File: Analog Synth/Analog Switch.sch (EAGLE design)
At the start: 15 parts, among them IC1 TL082P, Q1 J310, T3 2N3904

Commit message: working on senior design and analog switch
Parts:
- added R4: 100k, resistor:R-US_0204/2V
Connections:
- new net N$7: D3.A, IC1B.+IN, R4.1
- net +12V: now also R4.2; no longer D3.A, IC1B.-IN
- net N$4: now also IC1B.-IN; no longer IC1B.+IN
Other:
- moved on the sheet: IC1B
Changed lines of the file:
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@@
 <part name="P-1" library="supply1" deviceset="-12V" device=""/>
 <part name="SUPPLY5" library="supply2" deviceset="GND" device=""/>
+<part name="R4" library="resistor" deviceset="R-US_" device="0204/2V" value="100k"/>
 </parts>
 <sheets>
@@
 </instance>
 <instance part="SUPPLY3" gate="GND" x="10.16" y="40.64"/>
-<instance part="P+1" gate="1" x="17.78" y="66.04"/>
+<instance part="P+1" gate="1" x="17.78" y="73.66"/>
 <instance part="R6" gate="G$1" x="71.12" y="76.2" smashed="yes" rot="R270">
 <attribute name="NAME" x="67.5894" y="74.422" size="1.778" layer="95" rot="R90"/>
@@
 <instance part="SUPPLY7" gate="GND" x="111.76" y="35.56"/>
 <instance part="SUPPLY8" gate="GND" x="88.9" y="35.56"/>
-<instance part="IC1" gate="B" x="27.94" y="53.34"/>
+<instance part="IC1" gate="B" x="27.94" y="53.34" rot="MR180"/>
 <instance part="D3" gate="1" x="17.78" y="45.72" smashed="yes" rot="R270">
 <attribute name="NAME" x="19.5326" y="47.244" size="1.778" layer="95" rot="R270"/>
@@
 <instance part="P-1" gate="1" x="55.88" y="25.4"/>
 <instance part="SUPPLY5" gate="GND" x="40.64" y="25.4"/>
+<instance part="R4" gate="G$1" x="17.78" y="63.5" smashed="yes" rot="R90">
+<attribute name="NAME" x="13.7414" y="61.976" size="1.778" layer="95" rot="R90"/>
+<attribute name="VALUE" x="16.002" y="60.706" size="1.778" layer="96" rot="R90"/>
+</instance>
 </instances>
 <busses>
@@
 <net name="+12V" class="0">
 <segment>
-<pinref part="P+1" gate="1" pin="+12V"/>
-<wire x1="17.78" y1="50.8" x2="17.78" y2="63.5" width="0.1524" layer="91"/>
-<pinref part="IC1" gate="B" pin="-IN"/>
-<wire x1="20.32" y1="50.8" x2="17.78" y2="50.8" width="0.1524" layer="91"/>
-<pinref part="D3" gate="1" pin="A"/>
-<wire x1="17.78" y1="50.8" x2="17.78" y2="48.26" width="0.1524" layer="91"/>
-<junction x="17.78" y="50.8"/>
-</segment>
-<segment>
 <pinref part="U$1" gate="G$1" pin="P$1"/>
 <wire x1="99.06" y1="48.26" x2="93.98" y2="48.26" width="0.1524" layer="91"/>
@@
 <junction x="101.6" y="53.34"/>
 </segment>
+<segment>
+<pinref part="R4" gate="G$1" pin="2"/>
+<pinref part="P+1" gate="1" pin="+12V"/>
+<wire x1="17.78" y1="68.58" x2="17.78" y2="71.12" width="0.1524" layer="91"/>
+</segment>
 </net>
 <net name="N$6" class="0">
@@
 </segment>
 </net>
-<net name="N$4" class="0">
-<segment>
-<pinref part="GATE-IN" gate="J1" pin="P2"/>
-<pinref part="IC1" gate="B" pin="+IN"/>
-<wire x1="7.62" y1="55.88" x2="20.32" y2="55.88" width="0.1524" layer="91"/>
-</segment>
-</net>
 <net name="N$2" class="0">
 <segment>
@@
 </segment>
 </net>
+<net name="N$7" class="0">
+<segment>
+<pinref part="D3" gate="1" pin="A"/>
+<pinref part="R4" gate="G$1" pin="1"/>
+<wire x1="17.78" y1="58.42" x2="17.78" y2="50.8" width="0.1524" layer="91"/>
+<pinref part="IC1" gate="B" pin="+IN"/>
+<wire x1="17.78" y1="50.8" x2="17.78" y2="48.26" width="0.1524" layer="91"/>
+<wire x1="20.32" y1="50.8" x2="17.78" y2="50.8" width="0.1524" layer="91"/>
+<junction x="17.78" y="50.8"/>
+</segment>
+</net>
+<net name="N$4" class="0">
+<segment>
+<pinref part="IC1" gate="B" pin="-IN"/>
+<pinref part="GATE-IN" gate="J1" pin="P2"/>
+<wire x1="20.32" y1="55.88" x2="7.62" y2="55.88" width="0.1524" layer="91"/>
+</segment>
+</net>

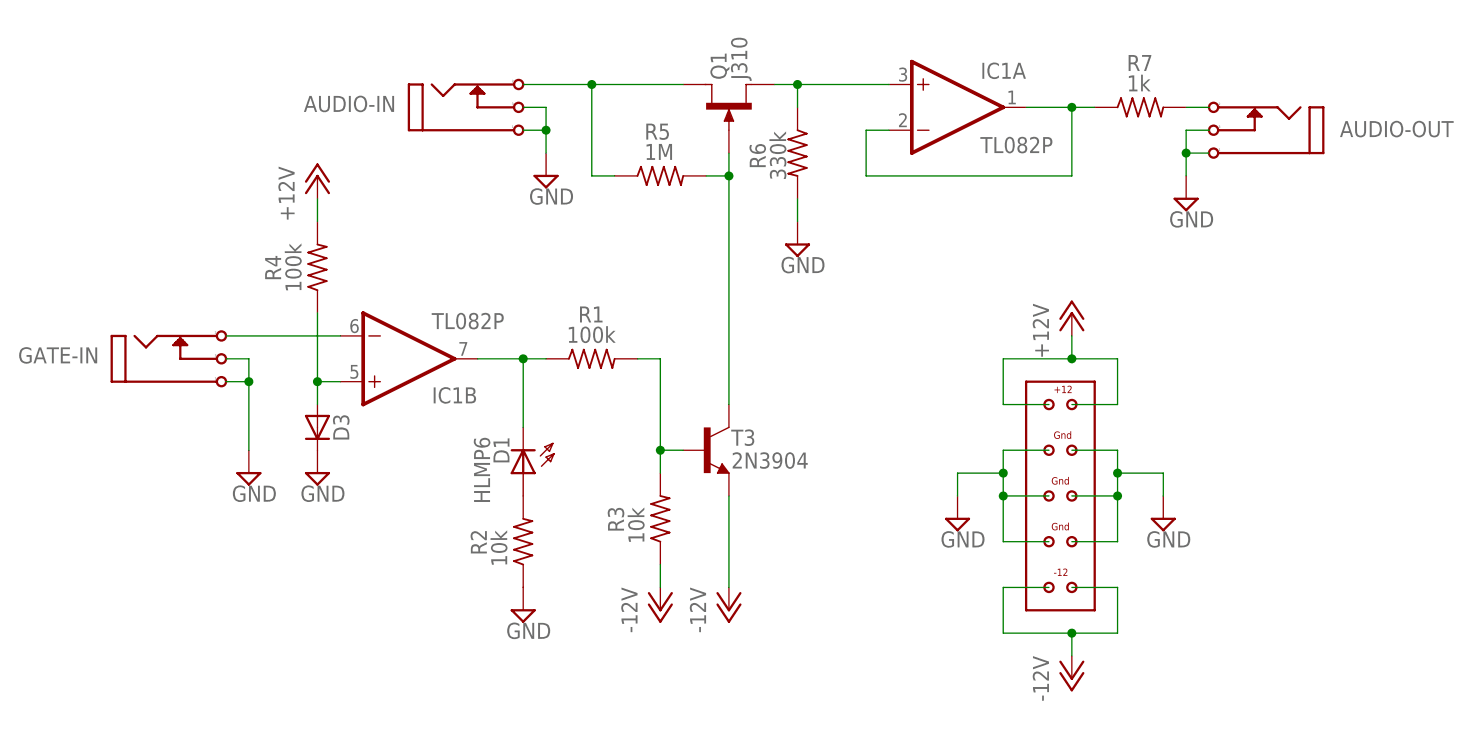
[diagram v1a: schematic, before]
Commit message: Updated the analog switch so that it doesn't suck so much. - Removed transistor and resistors. - Replaced with a diode to the gate of the JFET. - Changed grounding resistor from 330k to 56k. This was to reduce the amount that input audio "bleeds" into the output when it should be entirely disconnected.
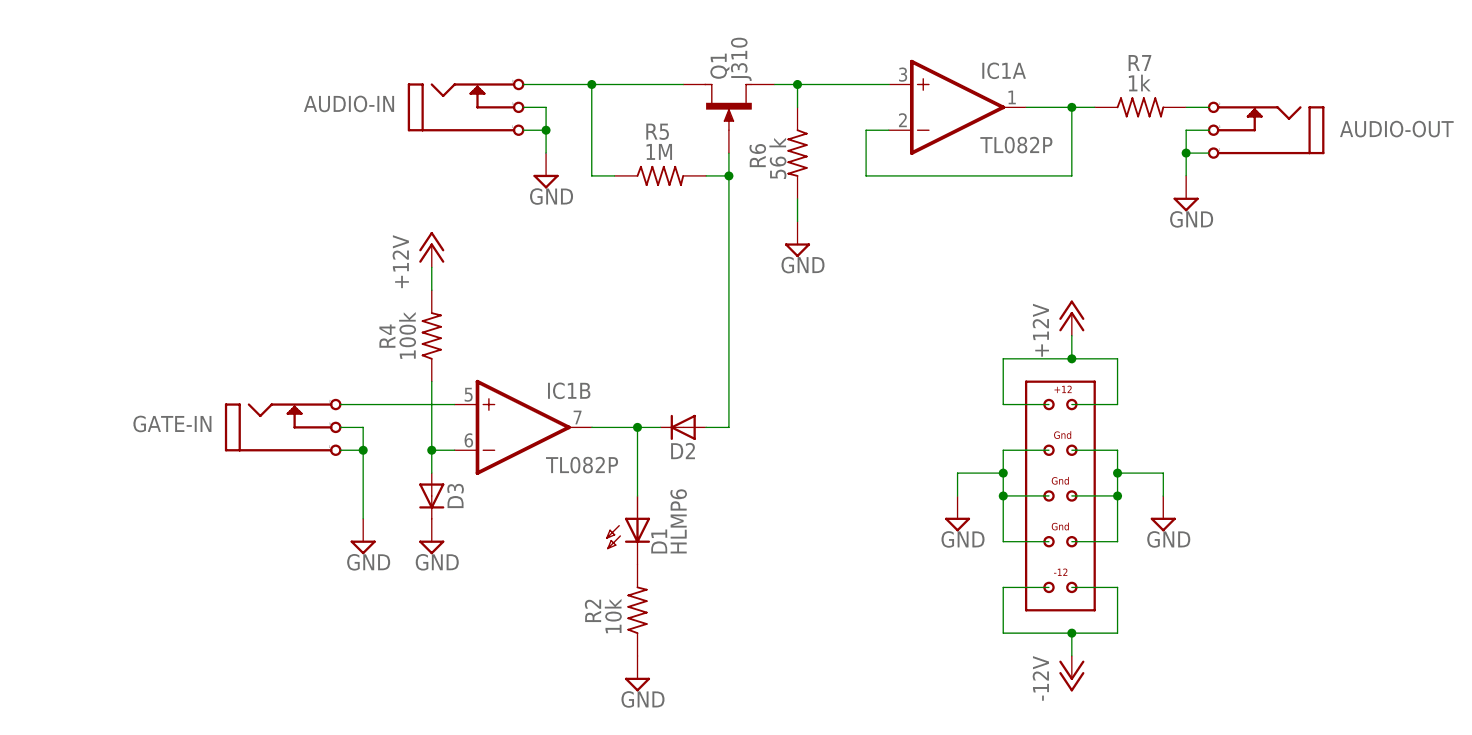
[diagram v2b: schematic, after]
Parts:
- removed R1: 100k, resistor:R-US_0204/2V
- removed R3: 10k, resistor:R-US_0204/2V
- removed T3: 2N3904, transistor:2N3904
- added D2: 1N4004, diode:1N4004
- R6: value 330k -> 56 k
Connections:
- removed net N$6: R1.2, R3.2, T3.B
- net -12V: no longer R3.1, T3.E
- net N$2: now also D1.A, D2.C; no longer D1.K, R1.1
- net N$3: now also D2.A; no longer T3.C
- net N$4: now also IC1B.+IN; no longer IC1B.-IN
- net N$5: now also D1.K; no longer D1.A
- net N$7: now also IC1B.-IN; no longer IC1B.+IN
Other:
- moved on the sheet: D1, D3, GATE-IN, IC1B, R2, R4
